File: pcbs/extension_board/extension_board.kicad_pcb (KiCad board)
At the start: 4 copper layers, 100 x 82.5 mm, 609 parts, among them J1 Conn_02x32_Counter_Clockwise, J2 Conn_02x03_Odd_Even, J3 Conn_01x05, J4 Conn_02x05_Odd_Even, J5 Barrel_Jack, J6 Conn_02x19_Odd_Even, J7 Conn_02x19_Odd_Even, J8 Conn_01x08, Q1 MMBT3904, Q10 MMBT3904, Q11 MMBT3904, Q12 MMBT3904, Q13 MMBT3904, Q14 MMBT3904, Q15 MMBT3904, Q16 MMBT3904, Q17 MMBT3904, Q18 MMBT3904, Q19 MMBT3904, Q2 MMBT3904, Q20 MMBT3904, Q21 MMBT3904, Q22 MMBT3904, Q23 MMBT3904, Q24 MMBT3904, Q25 MMBT3904, Q26 MMBT3904, Q27 MMBT3904, Q28 MMBT3904, Q29 MMBT3904, Q3 MMBT3904, Q30 MMBT3904, Q31 MMBT3904, Q32 MMBT3904, Q33 MMBT3904, Q34 MMBT3904, Q35 MMBT3904, Q36 MMBT3904, Q37 MMBT3904, Q38 MMBT3904, Q39 MMBT3904, Q4 MMBT3904, Q40 MMBT3904, Q41 MMBT3904, Q42 MMBT3904, Q43 MMBT3904, Q44 MMBT3904, Q45 MMBT3904, Q46 MMBT3904, Q47 MMBT3904, Q48 MMBT3904, Q49 MMBT3904, Q5 MMBT3904, Q50 MMBT3904, Q51 MMBT3904, Q52 MMBT3904, Q53 MMBT3904, Q54 MMBT3904, Q55 MMBT3904, Q56 MMBT3904, Q57 MMBT3904, Q58 MMBT3904, Q59 MMBT3904, Q6 MMBT3904, Q60 MMBT3904, Q61 MMBT3904, Q62 MMBT3904, Q63 MMBT3904, Q64 MMBT3904, Q7 MMBT3904, Q8 MMBT3904, Q9 MMBT3904, SW1 MY_SW_Push_Dual, SW2 Rotary_Encoder, SW3 Rotary_Encoder, U1 LM324QT, U10 LM324QT, U11 LM324QT, U12 LM324QT, U13 LM324QT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

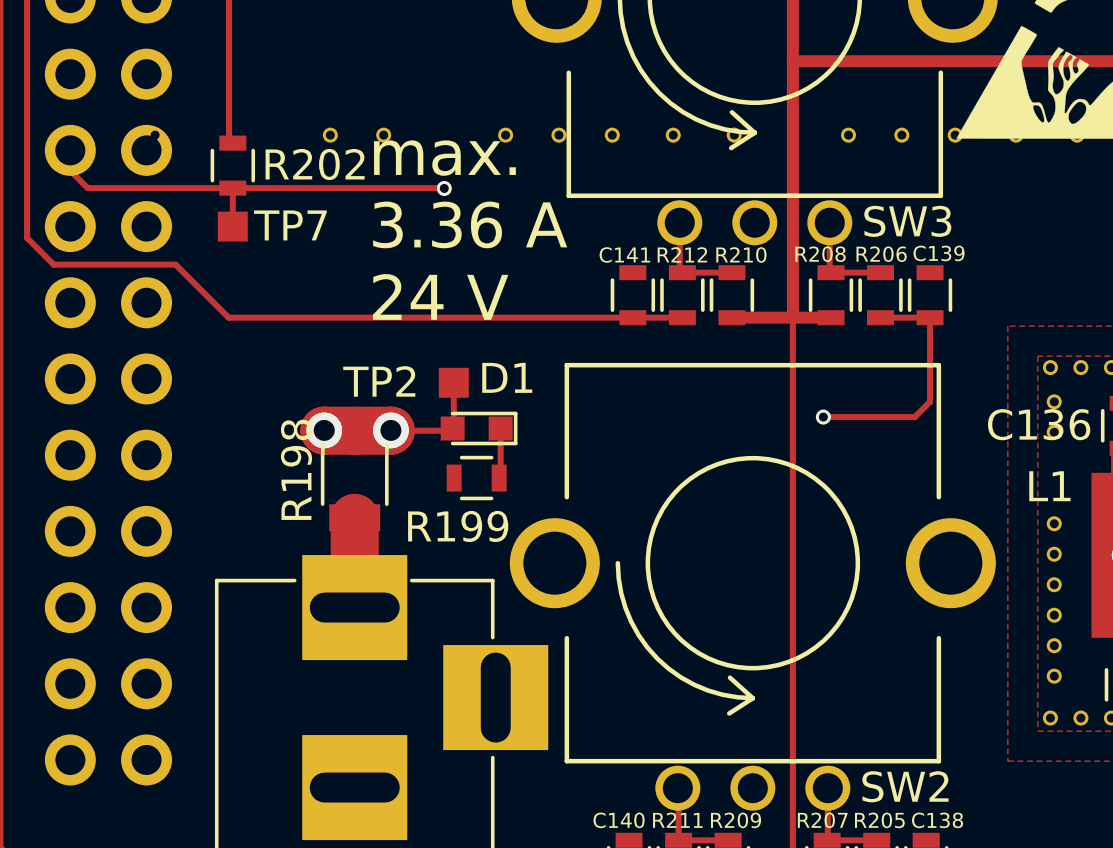
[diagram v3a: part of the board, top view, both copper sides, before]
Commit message: Updated current rating of extension board.
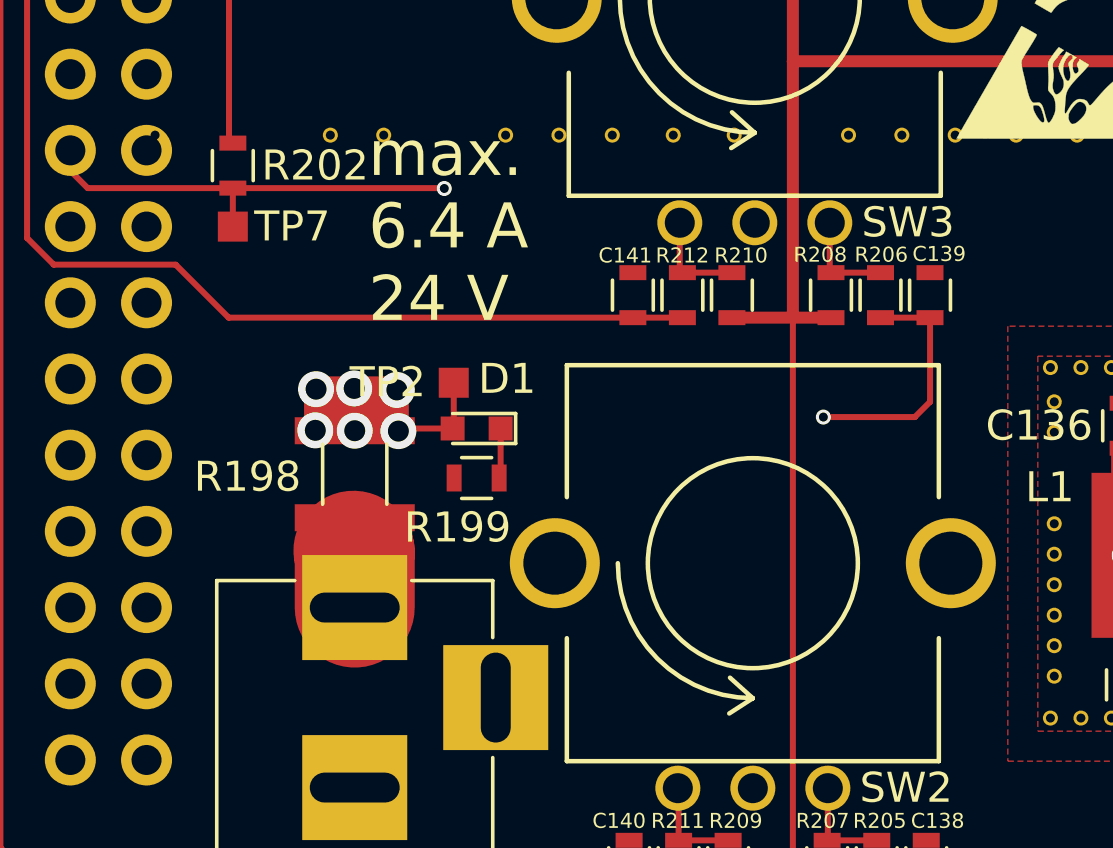
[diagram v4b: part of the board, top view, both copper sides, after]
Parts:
- R198: footprint Resistors_SMD:R_1206 -> MyResistors:R1206_4mm
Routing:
- net V18: track 61.2 -> 76.5 mm, vias 38 -> 42
- net Net-(J5-Pad1): track 2.99 -> 6.59 mm
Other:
- board text added: "max. 6.4 A 24 V"
- board text removed: "max. 3.36 A 24 V"

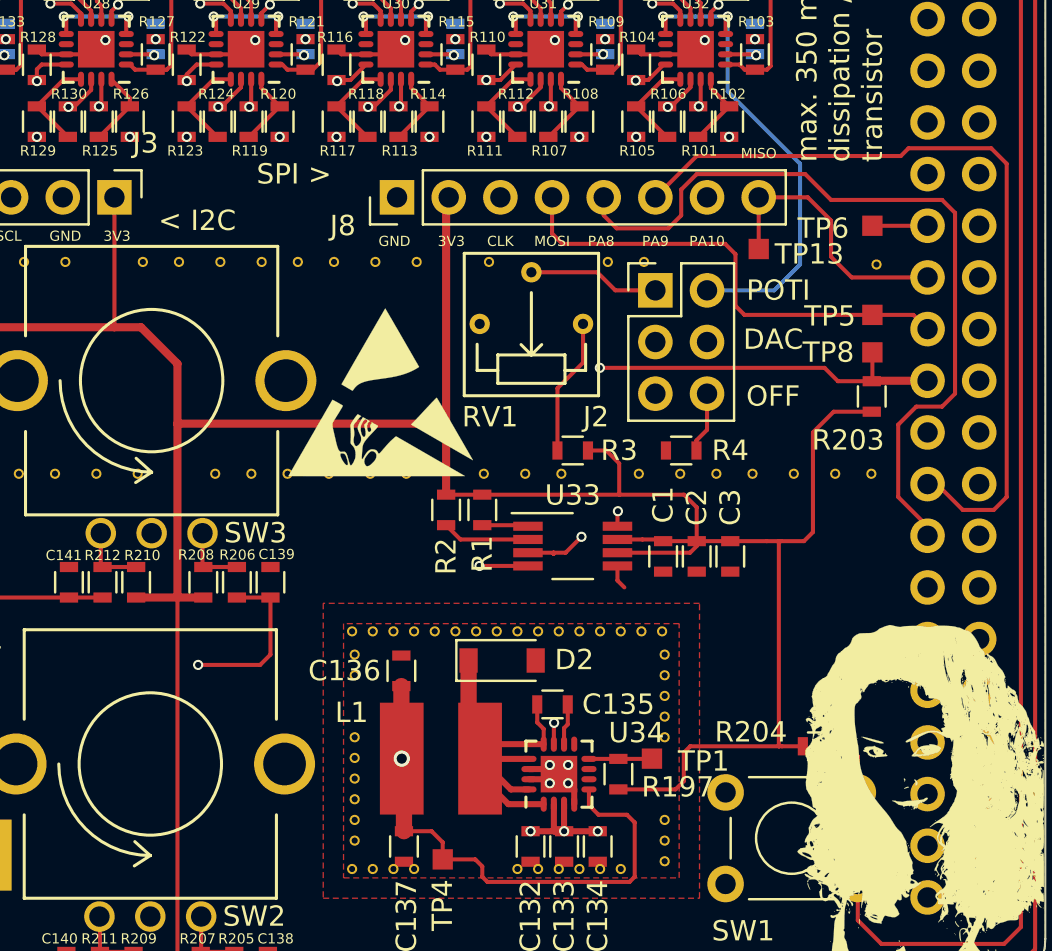
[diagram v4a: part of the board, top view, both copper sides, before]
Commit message: osPrintf works with signed and unsigned integers.
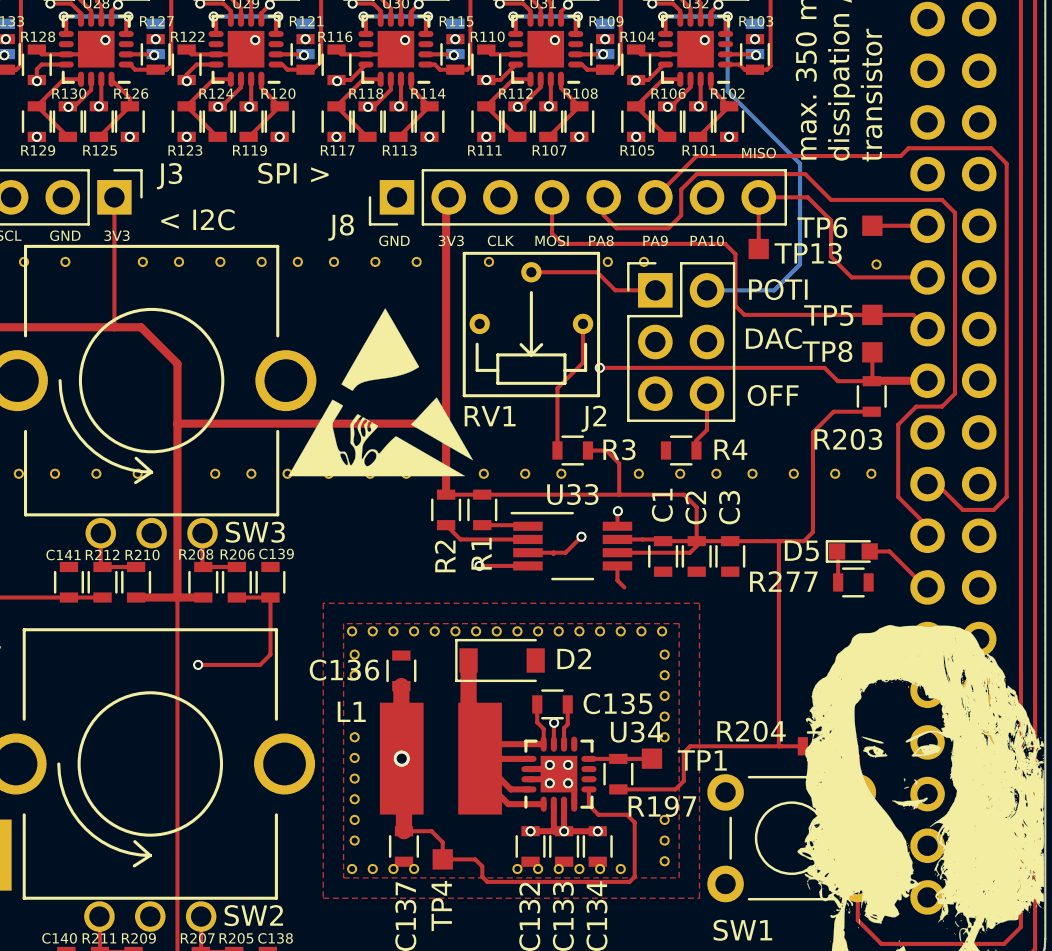
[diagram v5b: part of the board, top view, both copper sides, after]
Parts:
- added D5: LED, LEDs:LED_0603, F.Cu at (173.6, 107.5)
- added R277: 20R, Resistors_SMD:R_0603, F.Cu at (173.6, 109.0)
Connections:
- J2 pad 5: (no net) -> Net-(J2-Pad5)
- J6 pad 10: (no net) -> Net-(J6-Pad10)
- J6 pad 11: (no net) -> Net-(J6-Pad11)
- J6 pad 12: (no net) -> Net-(J6-Pad12)
- J6 pad 13: (no net) -> Net-(J6-Pad13)
- J6 pad 14: (no net) -> Net-(J6-Pad14)
- J6 pad 16: (no net) -> Net-(J6-Pad16)
- J6 pad 17: (no net) -> Net-(J6-Pad17)
- J6 pad 18: (no net) -> Net-(J6-Pad18)
- J6 pad 23: (no net) -> Net-(J6-Pad23)
- J6 pad 24: (no net) -> Net-(J6-Pad24)
- J6 pad 25: (no net) -> Net-(J6-Pad25)
- J6 pad 26: (no net) -> Net-(J6-Pad26)
- J6 pad 27: (no net) -> Net-(J6-Pad27)
- J6 pad 28: (no net) -> Net-(J6-Pad28)
- J6 pad 29: (no net) -> Net-(J6-Pad29)
- J6 pad 30: (no net) -> Net-(J6-Pad30)
- J6 pad 31: (no net) -> Net-(J6-Pad31)
- J6 pad 32: (no net) -> Net-(J6-Pad32)
- J6 pad 33: (no net) -> Net-(J6-Pad33)
- J6 pad 34: (no net) -> Net-(J6-Pad34)
- J6 pad 35: (no net) -> Net-(J6-Pad35)
- J6 pad 36: (no net) -> Net-(J6-Pad36)
- J6 pad 37: (no net) -> Net-(J6-Pad37)
- J6 pad 38: (no net) -> Net-(J6-Pad38)
- J6 pad 6: (no net) -> Net-(J6-Pad6)
- J6 pad 8: (no net) -> Net-(J6-Pad8)
- J6 pad 9: (no net) -> Net-(J6-Pad9)
- J7 pad 11: (no net) -> Net-(J7-Pad11)
- J7 pad 13: (no net) -> Net-(J7-Pad13)
- J7 pad 15: (no net) -> Net-(J7-Pad15)
- J7 pad 17: (no net) -> Net-(J7-Pad17)
- J7 pad 20: (no net) -> Net-(J7-Pad20)
- J7 pad 21: (no net) -> Net-(J7-Pad21)
- J7 pad 23: (no net) -> Net-(J7-Pad23)
- J7 pad 25: (no net) -> Net-(J7-Pad25)
- J7 pad 26: (no net) -> PB10
- J7 pad 27: (no net) -> Net-(J7-Pad27)
- J7 pad 28: (no net) -> Net-(J7-Pad28)
- J7 pad 29: (no net) -> Net-(J7-Pad29)
- J7 pad 3: (no net) -> Net-(J7-Pad3)
- J7 pad 30: (no net) -> Net-(J7-Pad30)
- J7 pad 31: (no net) -> Net-(J7-Pad31)
- J7 pad 32: (no net) -> Net-(J7-Pad32)
- J7 pad 33: (no net) -> Net-(J7-Pad33)
- J7 pad 35: (no net) -> Net-(J7-Pad35)
- J7 pad 36: (no net) -> Net-(J7-Pad36)
- J7 pad 37: (no net) -> Net-(J7-Pad37)
- J7 pad 38: (no net) -> Net-(J7-Pad38)
- J7 pad 4: (no net) -> Net-(J7-Pad4)
- J7 pad 5: (no net) -> Net-(J7-Pad5)
- J7 pad 6: (no net) -> Net-(J7-Pad6)
- J7 pad 7: (no net) -> Net-(J7-Pad7)
- J7 pad 8: (no net) -> Net-(J7-Pad8)
- J7 pad 9: (no net) -> Net-(J7-Pad9)
- U34 pad 6: (no net) -> Net-(U34-Pad6)
- U34 pad 7: (no net) -> Net-(U34-Pad7)
- U34 pad 9: (no net) -> Net-(U34-Pad9)
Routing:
- net PB10: track 0.00 -> 3.58 mm
- net Net-(D5-Pad1): track 0.00 -> 1.54 mm
